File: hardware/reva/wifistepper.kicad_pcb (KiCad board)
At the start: 2 copper layers, 92 x 52 mm, 57 parts, among them J1 Barrel_Jack_Switch, J2 Screw_Terminal, J3 Conn_01x06, J4 Conn_01x06, J5 Conn_01x04, U1 ESP-WROOM-02, U2 powerSTEP01, U3 MAX15062A, U4 ATECC508A

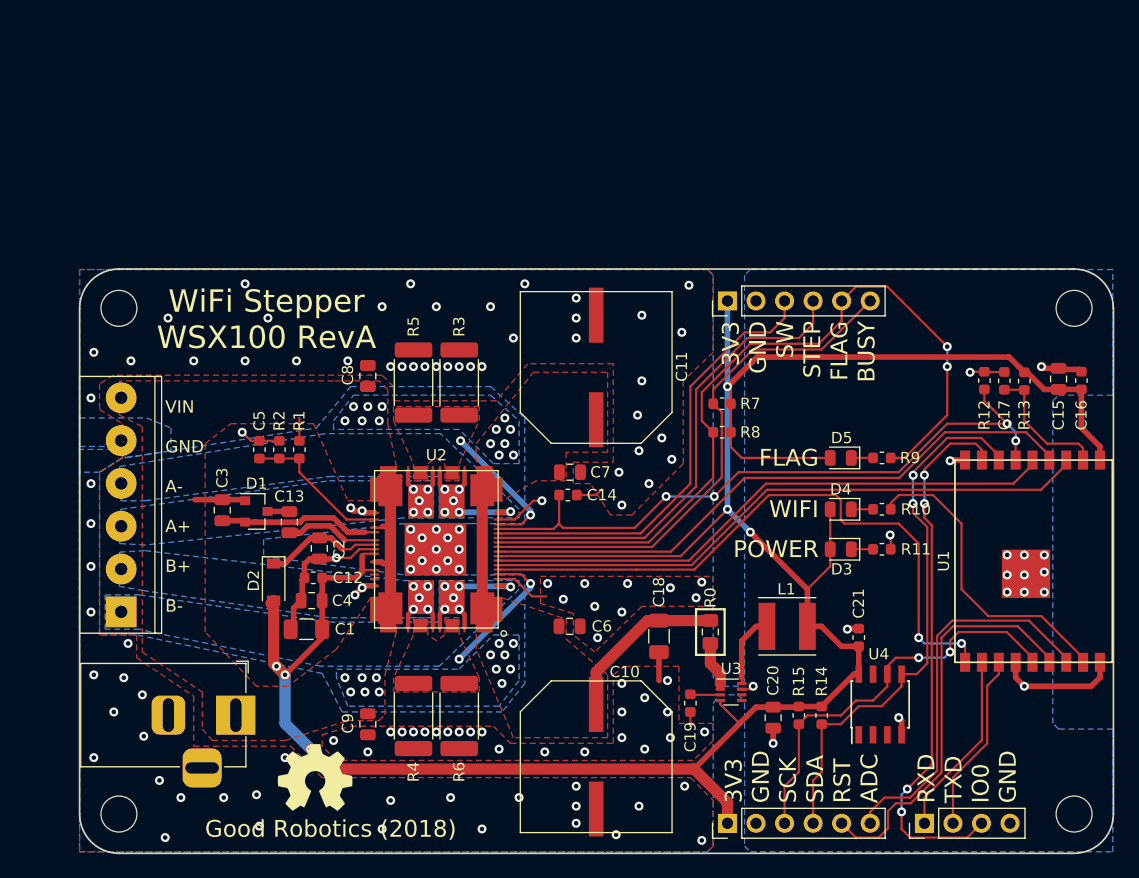
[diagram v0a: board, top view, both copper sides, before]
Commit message: Webpage development, rework of RevA
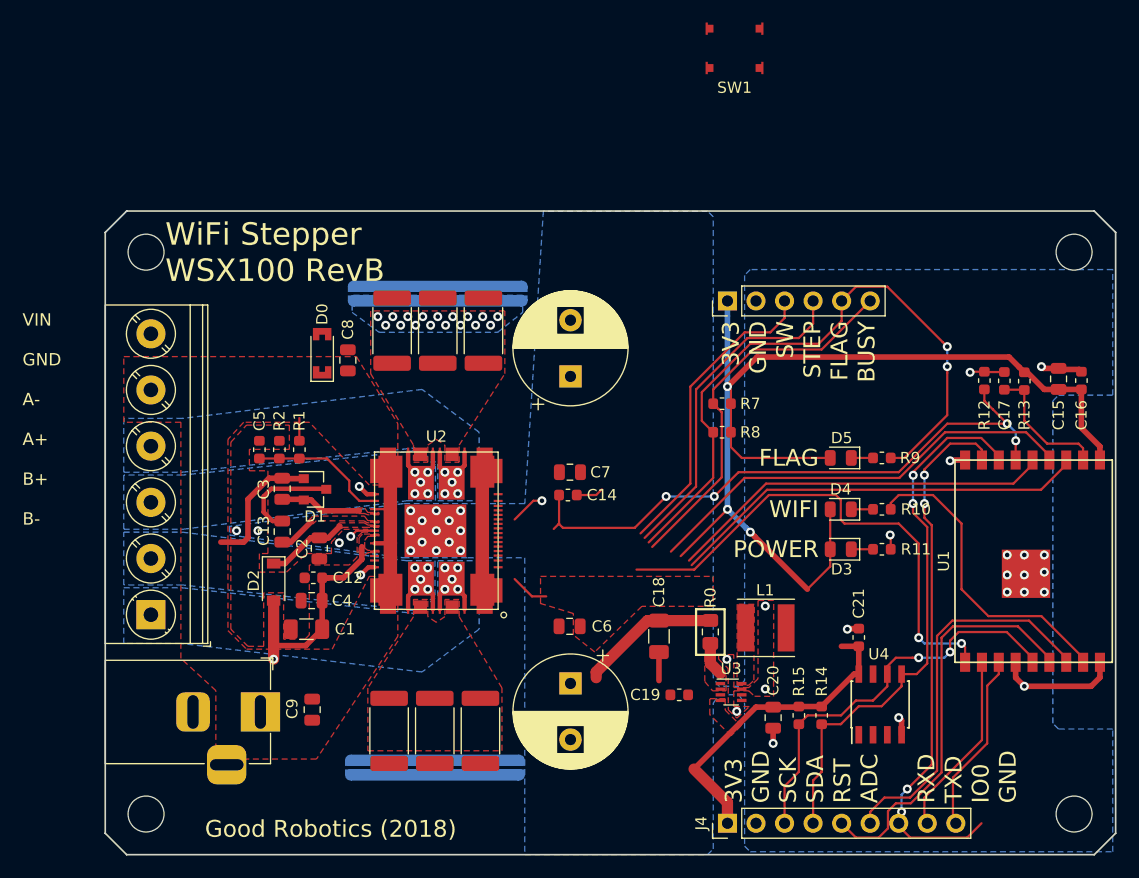
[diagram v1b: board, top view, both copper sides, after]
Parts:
- removed J5: Conn_01x04, Connector_PinHeader_2.54mm:PinHeader_1x04_P2.54mm_Vertical
- removed R3, R4, R5, R6: 0.2, Resistor_SMD:R_2512_6332Metric
- removed the REF** at (52.5, 111.8)
- added D0: RPOL, Klofas-Passives:D_SOD80, F.Cu at (53.1, 74.0)
- added JP1: Jumper_2_Open, Klofas-Connectors:STpowerSTEP01_JMP, B.Cu at (63.4, 68.7)
- added JP2: Jumper_2_Open, Klofas-Connectors:STpowerSTEP01_JMP, B.Cu at (63.1, 110.9)
- added RS1: 0.06, Resistor_SMD:R_2512_6332Metric, F.Cu at (59.3, 72.0)
- added RS2: 0.06, Resistor_SMD:R_2512_6332Metric, F.Cu at (63.4, 72.0)
- added RS3: 0.06, Resistor_SMD:R_2512_6332Metric, F.Cu at (67.4, 72.0)
- added RS4: 0.06, Resistor_SMD:R_2512_6332Metric, F.Cu at (59.0, 107.6)
- added RS5: 0.06, Resistor_SMD:R_2512_6332Metric, F.Cu at (63.1, 107.6)
- added RS6: 0.06, Resistor_SMD:R_2512_6332Metric, F.Cu at (67.2, 107.6)
- added SW1: SW_SPST, Klofas-Passives:TL3315NF100Q, F.Cu at (89.8, 46.9)
- C10, C11: footprint Klofas-Passives:Capacitor_SMD-Panasonic_H13 -> Capacitor_THT:CP_Radial_D10.0mm_P5.00mm
- J2: footprint Klofas-Connectors:Phoenix_Screw_Terminal-MKDS_1,6-P3.81x06 -> TerminalBlock_Phoenix:TerminalBlock_Phoenix_PT-1,5-6-5.0-H_1x06_P5.00mm_Horizontal
- J4: value Conn_01x06 -> Conn_01x09; footprint Connector_PinHeader_2.54mm:PinHeader_1x06_P2.54mm_Vertical -> Connector_PinHeader_2.54mm:PinHeader_1x09_P2.54mm_Vertical
- moved C10 6.91 mm to (75.2, 103.4), turned to 270 degrees
- moved C3 5.66 mm to (49.5, 86.1)
- moved D1 5.58 mm to (52.5, 86.1)
- moved REF** 5.55 mm to (37.4, 65.0)
- moved C9 5.12 mm to (52.2, 105.7)
- moved REF** 5.00 mm to (120.0, 65.0)
- moved J2 2.66 mm to (37.8, 97.3)
- moved C11 2.42 mm to (75.2, 76.1), turned to 90 degrees
- moved REF** 2.41 mm to (37.4, 115.0)
- moved C8 2.26 mm to (55.4, 74.6)
- moved J1 2.21 mm to (47.6, 105.9)
- moved L1 1.90 mm to (92.6, 98.4)
- moved U2 1.65 mm to (63.2, 89.8)
- moved C19 1.23 mm to (84.9, 104.4), turned to 180 degrees
- moved C13 1.05 mm to (49.5, 89.9)
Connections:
- J1 pad 3: GND -> Net-(J1-Pad3)
- J2 pad 5: GND -> VIN
- J2 pad 6: VIN -> GND
- J4 pad 5: WIFI_RST -> WIFI_ADC
- J4 pad 6: WIFI_ADC -> WIFI_RST
- U2 pad 63: (no net) -> Net-(U2-Pad63)
- U2 pad 64: (no net) -> Net-(U2-Pad64)
- U3 pad 5: (no net) -> Net-(U3-Pad5)
- U3 pad 6: (no net) -> Net-(U3-Pad6)
- U4 pad 1: (no net) -> Net-(U4-Pad1)
- U4 pad 2: (no net) -> Net-(U4-Pad2)
- U4 pad 3: (no net) -> Net-(U4-Pad3)
- U4 pad 7: (no net) -> Net-(U4-Pad7)
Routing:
- net +3V3: track 221.9 -> 146.4 mm, vias 7 -> 4
- net GND: track 58.0 -> 38.2 mm, vias 137 -> 39
- net SM_CLK: track 54.7 -> 37.4 mm
- net SM_SI: track 51.5 -> 34.5 mm
- net SM_SO: track 54.7 -> 39.3 mm
- net SM_BUSY: track 47.8 -> 34.1 mm
- net SM_FLAG: track 71.2 -> 57.8 mm
- net SM_STCLK: track 43.0 -> 30.0 mm
- net SM_SW: track 40.0 -> 27.3 mm
- net Net-(JP2-Pad1): track 12.6 -> 0.00 mm, vias 2 -> 0
- net Net-(JP1-Pad1): track 12.4 -> 0.00 mm, vias 2 -> 17
- net SM_CS: track 57.2 -> 44.9 mm
- net Net-(C13-Pad2): track 1.95 -> 9.25 mm
- net Net-(C3-Pad1): track 14.3 -> 7.29 mm
- net VIN: track 43.2 -> 50.2 mm, vias 26 -> 0
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- added copper zone on F.Cu, net +3V3
- added copper zone on F.Cu, net Net-(C13-Pad1)
- added copper zone on F.Cu, net Net-(C2-Pad1)
- added copper zone on F.Cu, net Net-(C3-Pad1)
- added copper zone on B.Cu, net Net-(JP1-Pad1)
- added copper zone on F.Cu, net Net-(L1-Pad2)
- added copper zone on F.Cu, net Net-(R0-Pad1)
- removed copper zone on B.Cu, net VIN
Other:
- board size 92 x 52 mm -> 89.9 x 57.3 mm
- board text added: "WiFi Stepper WSX100 RevB"
- board text removed: "WiFi Stepper WSX100 RevA"

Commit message: Rev B design complete
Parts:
- added C22: 0.1uF, Capacitor_SMD:C_0603_1608Metric, F.Cu at (75.7, 89.0)
- added J5: Conn_01x02, Connector_PinHeader_2.54mm:PinHeader_1x02_P2.54mm_Vertical, F.Cu at (77.0, 92.6)
- moved SW1 61.9 mm to (102.7, 107.4), turned to 180 degrees
- moved D0 36.3 mm to (55.6, 110.2), turned to 270 degrees
- moved U1 21.5 mm to (91.4, 80.7)
- moved C16 20.2 mm to (103.0, 66.6)
- moved C17 20.2 mm to (96.1, 66.7)
- moved C15 20.2 mm to (101.0, 66.5)
- moved R13 20.2 mm to (97.9, 66.7)
- moved R12 20.1 mm to (94.4, 66.7)
- moved R9 18.0 mm to (87.4, 92.5), turned to 180 degrees
- moved D5 16.6 mm to (104.1, 99.2)
- moved R7 16.1 mm to (95.2, 63.7)
- moved D4 14.8 mm to (104.1, 101.9)
- moved R8 12.8 mm to (84.9, 93.2), turned to 90 degrees
- moved REF** 12.3 mm to (107.7, 65.0)
- moved REF** 12.3 mm to (107.7, 115.0)
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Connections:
- J1 pad 3: Net-(J1-Pad3) -> (no net)
- J4 pad 5: WIFI_ADC -> WIFI_RST
- J4 pad 6: WIFI_RST -> WIFI_ADC
- U2 pad 63: Net-(U2-Pad63) -> (no net)
- U2 pad 64: Net-(U2-Pad64) -> (no net)
- U3 pad 5: Net-(U3-Pad5) -> (no net)
- U3 pad 6: Net-(U3-Pad6) -> (no net)
- U4 pad 1: Net-(U4-Pad1) -> (no net)
- U4 pad 2: Net-(U4-Pad2) -> (no net)
- U4 pad 3: Net-(U4-Pad3) -> (no net)
- U4 pad 7: Net-(U4-Pad7) -> (no net)
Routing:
- net +3V3: track 146.4 -> 190.7 mm, vias 4 -> 9
- net AUTH_SDA: track 48.9 -> 70.4 mm, vias 2 -> 0
- net WIFI_CONN: track 27.8 -> 7.54 mm
- net SM_CS: track 44.9 -> 25.4 mm
- net Net-(D5-Pad1): track 1.94 -> 19.6 mm, vias 0 -> 2
- net PROG_RX: track 16.4 -> 32.9 mm, vias 0 -> 1
- net PROG_TX: track 16.0 -> 31.5 mm, vias 0 -> 1
- net GND: track 38.2 -> 22.8 mm, vias 39 -> 248
- net SM_CLK: track 37.4 -> 50.7 mm, vias 0 -> 2
- net AUTH_SCK: track 36.5 -> 49.8 mm
- net Net-(JP2-Pad1): track 0.00 -> 12.6 mm, vias 0 -> 19
- net Net-(JP1-Pad1): track 0.00 -> 12.2 mm, vias 17 -> 19
- net SM_SI: track 34.5 -> 46.0 mm
- net SM_BUSY: track 34.1 -> 45.5 mm
- net SM_RST: track 54.5 -> 44.5 mm
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- added copper zone on F.Cu, net Net-(C19-Pad1)
- added copper zone on B.Cu, net Net-(JP2-Pad1)
- added copper zone on B.Cu, net VIN
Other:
- board size 89.9 x 57.3 mm -> 77.6 x 57.3 mm
- board text added: "3V3 GND SCK SDA RST ADC BOOT RX TX"
- board text added: "50V MAX"
- board text added: "85V MAX"
- board text added: "GND"
- board text added: "GND VIN A- A+ B+ B-"
- board text added: "RESET"
- board text added: "Short for Voltage Mode"
- board text added: "VIN"
- board text added: "WSX100 RevB"
- board text added: "WiFi Stepper"
- board text removed: "3V3 GND SCK SDA RST ADC"
- board text removed: "RXD TXD IO0 GND"
- board text removed: "VIN GND A- A+ B+ B-"
- board text removed: "WiFi Stepper WSX100 RevB"
